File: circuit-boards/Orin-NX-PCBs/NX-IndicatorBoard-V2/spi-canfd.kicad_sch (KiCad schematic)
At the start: 9 parts, among them U3 MCP2518FD-xQBB, U5 40MHz, U7 MCP2558FD

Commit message: Check in of NX Adapter and Indicator boards.  Complete pending review
Signed-off-by: Scott <sgberman1@gmail.com>
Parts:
- removed C2: 0.1uF-10%-50V-0603, Capacitor_SMD:C_0603_1608Metric, symbol Device:C
- added C3: 0.1uF-10%-50V-0805, Capacitor_SMD:C_0805_2012Metric, symbol Device:C
- C2: renamed from C4; value 0.1uF-10%-50V-0603 -> 0.1uF-10%-50V-0805; footprint Capacitor_SMD:C_0603_1608Metric -> Capacitor_SMD:C_0805_2012Metric; DIST P/N 1276-1000-1-ND -> 311-1140-1-ND; MFG Samsung Electro-Mechanics -> YAGEO; MFG P/N CL10B104KB8NNNC -> CC0805KRX7R9BB104
- C6, C8: value 0.1uF-10%-50V-0603 -> 0.1uF-10%-50V-0805; footprint Capacitor_SMD:C_0603_1608Metric -> Capacitor_SMD:C_0805_2012Metric; DIST P/N 1276-1000-1-ND -> 311-1140-1-ND; MFG Samsung Electro-Mechanics -> YAGEO; MFG P/N CL10B104KB8NNNC -> CC0805KRX7R9BB104
- U5: renamed from U7; footprint Package_DFN_QFN:DFN-8-1EP_3x3mm_P0.65mm_EP1.55x2.4mm -> Package_SO:SO-8_3.9x4.9mm_P1.27mm; DIST P/N MCP2558FDT-H/MFCT-ND -> MCP2558FD-H/SN-ND; MFG P/N MCP2558FDT-H/MF -> MCP2558FD-H/SN
- U6: renamed from U3; value MCP2518FD-xQBB -> MCP2518FDT-H/SL; footprint Package_DFN_QFN:DFN-14-1EP_3x4.5mm_P0.65mm_EP1.65x4.25mm -> Package_SO:SO-14_3.9x8.65mm_P1.27mm; DIST P/N MCP2518FDT-E/QBBCT-ND -> MCP2518FDT-H/SLCT-ND; MFG P/N MCP2518FDT-E/QBB -> MCP2518FDT-H/SL
- renumbered D2 to D10, U5 to U7
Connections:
- net +3V3: now also C6.1
- net +5V: now also C3.1; no longer C6.1
- net GND: now also C3.2; no longer U5.9 (EP), U6.15 (VSS)

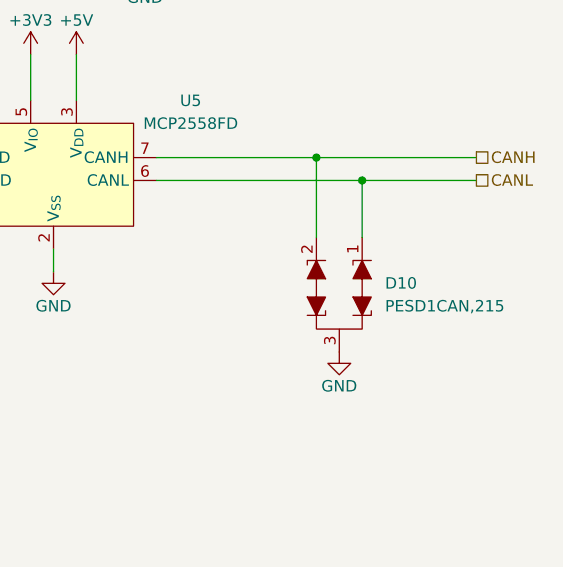
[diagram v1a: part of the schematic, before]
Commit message: Checkin of NX Indicator board 2x CAN FD + 6 LEDs
Signed-off-by: Scott <sgberman1@gmail.com>
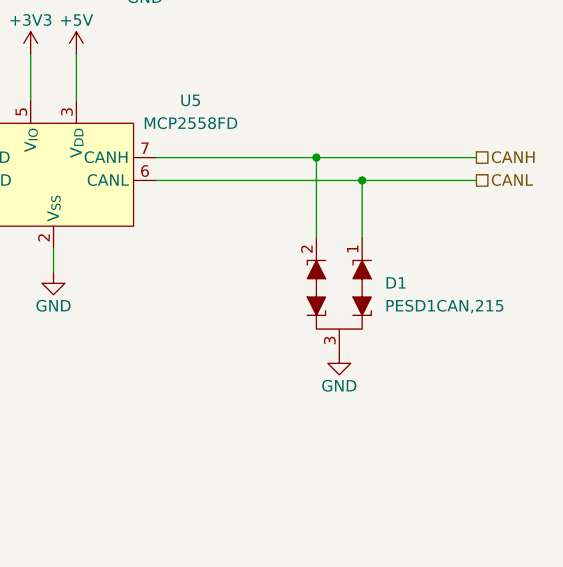
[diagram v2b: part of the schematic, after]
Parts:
- renumbered D10 to D1
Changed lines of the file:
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@@
 	(title_block
 		(title "NX Indicator Board V2")
-		(date "2024-07-21")
+		(date "2024-07-28")
 		(rev "2")
 		(company "971 Spartan Robotics")
@@
 		(dnp no)
 		(fields_autoplaced yes)
-		(property "Reference" "D10"
+		(property "Reference" "D1"
 			(at 262.89 124.4599 90)
 			(effects
@@
 			(project "NX-IndicatorBoard"
 				(path "/b2b9b2ba-ad3f-4e65-98f2-b291a62e1006/aabb8c17-0b3a-4fc6-ab19-23fda34518d0"
-					(reference "D10")
+					(reference "D1")
 					(unit 1)
 				)
 				(path "/b2b9b2ba-ad3f-4e65-98f2-b291a62e1006/d7bf2cad-628f-4840-beb5-4ea56fd6a130"
-					(reference "D11")
+					(reference "D2")
 					(unit 1)
 				)
